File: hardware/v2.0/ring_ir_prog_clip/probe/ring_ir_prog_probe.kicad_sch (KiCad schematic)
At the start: 9 parts, among them J1 AVR_ISP_6, J2 GND_lead_to_anvil, P1 Pogo TP1 PB0, P2 Pogo TP2 PB1, P3 Pogo TP3 PB2, P4 Pogo TP4 PB3, P5 Pogo TP5 PB4, P6 Pogo TP6 PB5, P9 Pogo TP9 VCC

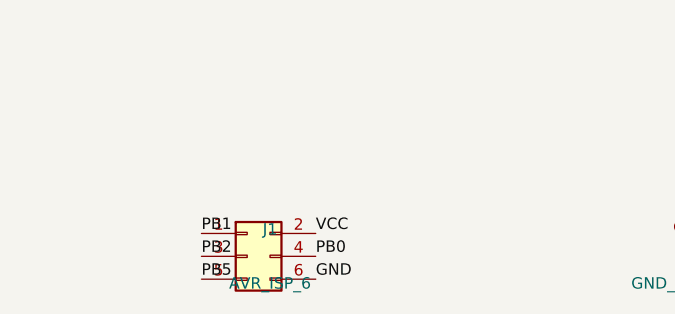
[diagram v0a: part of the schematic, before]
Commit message: Use SMD ISP header and STEP-based clip assembly renders
Regenerate checked clip PCBs, 2D drawings, actual STEP assemblies and assembly media. Document IR ISP wiring, the anvil ground return and target-specific SWD voltage-reference requirements.

Co-authored-by: Copilot <223556219+Copilot@users.noreply.github.com>
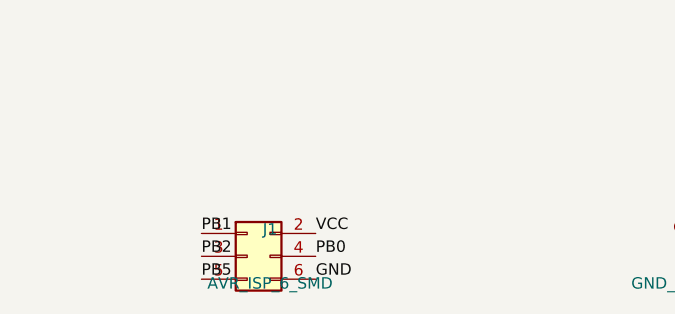
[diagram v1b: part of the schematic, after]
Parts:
- J1: value AVR_ISP_6 -> AVR_ISP_6_SMD; footprint Connector_PinHeader_2.54mm:PinHeader_2x03_P2.54mm_Vertical -> Connector_PinHeader_2.54mm:PinHeader_2x03_P2.54mm_Vertical_SMD
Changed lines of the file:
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@@
 			)
 		)
-		(property "Value" "AVR_ISP_6"
+		(property "Value" "AVR_ISP_6_SMD"
 			(at 63.5 112.22 0)
 			(show_name no)
@@
 			)
 		)
-		(property "Footprint" "Connector_PinHeader_2.54mm:PinHeader_2x03_P2.54mm_Vertical"
+		(property "Footprint" "Connector_PinHeader_2.54mm:PinHeader_2x03_P2.54mm_Vertical_SMD"
 			(at 63.5 114.22 0)
 			(hide yes)
